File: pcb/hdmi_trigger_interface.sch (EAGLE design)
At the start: 60 parts, among them U1 TPD12S016PWR, U2 TPD12S016PWR, X1 87438-06, X2 87438-06, Y1 SI514

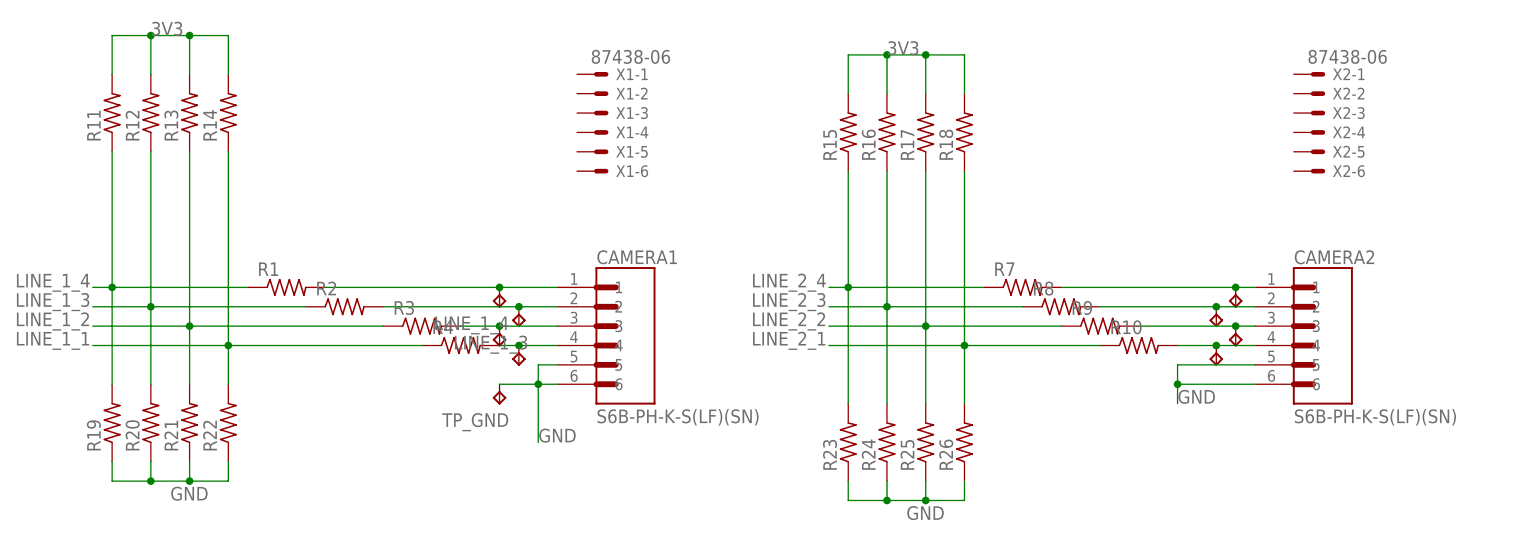
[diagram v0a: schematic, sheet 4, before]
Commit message: finished routing with new spacing and layout.
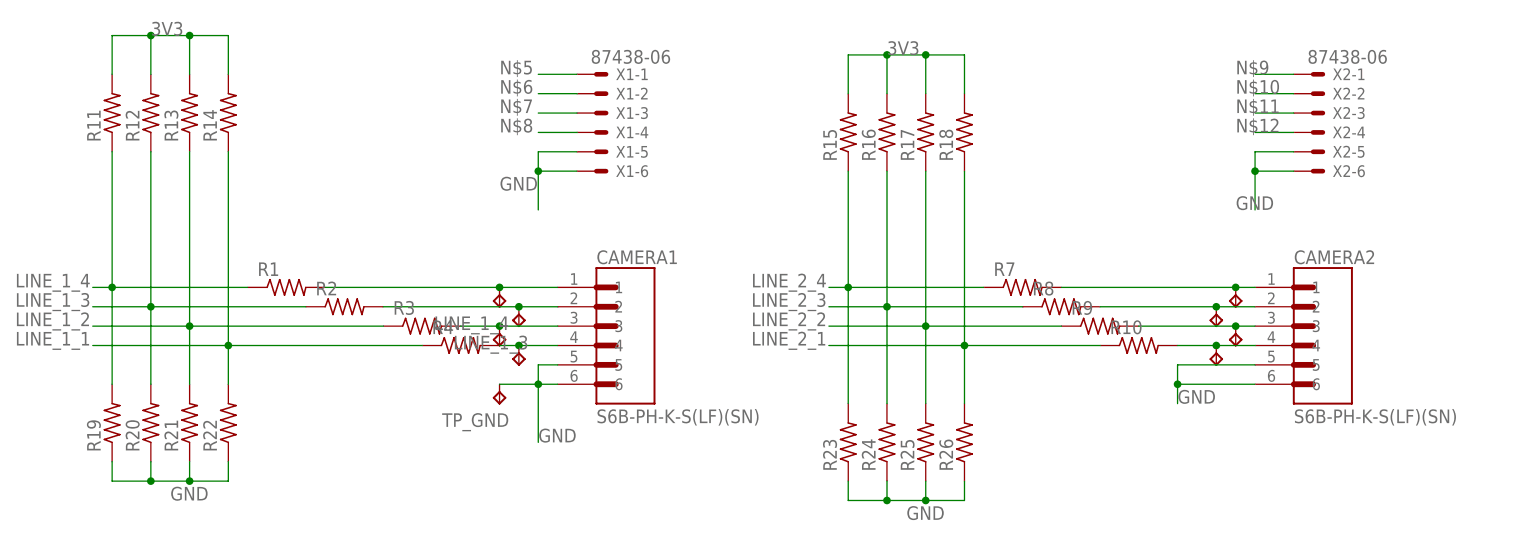
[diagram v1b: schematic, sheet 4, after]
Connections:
- net GND: now also X1-5.S, X1-6.S, X2-5.S, X2-6.S
- net N$10: now also X2-2.S
- net N$11: now also X2-3.S
- net N$12: now also X2-4.S
- net N$5: now also X1-1.S
- net N$6: now also X1-2.S
- net N$7: now also X1-3.S
- net N$8: now also X1-4.S
- net N$9: now also X2-1.S
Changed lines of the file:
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@@
 <label x="162.56" y="25.4" size="1.778" layer="95"/>
+</segment>
+<segment>
+<pinref part="X1" gate="-5" pin="S"/>
+<wire x1="83.82" y1="58.42" x2="78.74" y2="58.42" width="0.1524" layer="91"/>
+<wire x1="78.74" y1="58.42" x2="78.74" y2="55.88" width="0.1524" layer="91"/>
+<pinref part="X1" gate="-6" pin="S"/>
+<wire x1="78.74" y1="55.88" x2="83.82" y2="55.88" width="0.1524" layer="91"/>
+<wire x1="78.74" y1="55.88" x2="78.74" y2="50.8" width="0.1524" layer="91"/>
+<junction x="78.74" y="55.88"/>
+<label x="73.66" y="53.34" size="1.778" layer="95"/>
+</segment>
+<segment>
+<pinref part="X2" gate="-5" pin="S"/>
+<wire x1="177.8" y1="58.42" x2="172.72" y2="58.42" width="0.1524" layer="91"/>
+<wire x1="172.72" y1="58.42" x2="172.72" y2="55.88" width="0.1524" layer="91"/>
+<pinref part="X2" gate="-6" pin="S"/>
+<wire x1="172.72" y1="55.88" x2="177.8" y2="55.88" width="0.1524" layer="91"/>
+<wire x1="172.72" y1="55.88" x2="172.72" y2="50.8" width="0.1524" layer="91"/>
+<junction x="172.72" y="55.88"/>
+<label x="170.18" y="50.8" size="1.778" layer="95"/>
 </segment>
 </net>
@@
 <pinref part="CAMERA1" gate="G$1" pin="1"/>
 </segment>
+<segment>
+<pinref part="X1" gate="-1" pin="S"/>
+<wire x1="83.82" y1="68.58" x2="78.74" y2="68.58" width="0.1524" layer="91"/>
+<label x="73.66" y="68.58" size="1.778" layer="95"/>
+</segment>
 </net>
 <net name="N$6" class="0">
@@
 <pinref part="CAMERA1" gate="G$1" pin="2"/>
 </segment>
+<segment>
+<pinref part="X1" gate="-2" pin="S"/>
+<wire x1="83.82" y1="66.04" x2="78.74" y2="66.04" width="0.1524" layer="91"/>
+<label x="73.66" y="66.04" size="1.778" layer="95"/>
+</segment>
 </net>
 <net name="N$7" class="0">
@@
 <pinref part="CAMERA1" gate="G$1" pin="3"/>
 </segment>
+<segment>
+<pinref part="X1" gate="-3" pin="S"/>
+<wire x1="83.82" y1="63.5" x2="78.74" y2="63.5" width="0.1524" layer="91"/>
+<label x="73.66" y="63.5" size="1.778" layer="95"/>
+</segment>
 </net>
 <net name="N$8" class="0">
@@
 <pinref part="CAMERA1" gate="G$1" pin="4"/>
 </segment>
+<segment>
+<pinref part="X1" gate="-4" pin="S"/>
+<wire x1="83.82" y1="60.96" x2="78.74" y2="60.96" width="0.1524" layer="91"/>
+<label x="73.66" y="60.96" size="1.778" layer="95"/>
+</segment>
 </net>
 <net name="N$9" class="0">
@@
 <pinref part="CAMERA2" gate="G$1" pin="1"/>
 </segment>
+<segment>
+<pinref part="X2" gate="-1" pin="S"/>
+<wire x1="177.8" y1="68.58" x2="172.72" y2="68.58" width="0.1524" layer="91"/>
+<label x="170.18" y="68.58" size="1.778" layer="95"/>
+</segment>
 </net>
 <net name="N$10" class="0">
@@
 <pinref part="CAMERA2" gate="G$1" pin="2"/>
 </segment>
+<segment>
+<pinref part="X2" gate="-2" pin="S"/>
+<wire x1="177.8" y1="66.04" x2="172.72" y2="66.04" width="0.1524" layer="91"/>
+<label x="170.18" y="66.04" size="1.778" layer="95"/>
+</segment>
 </net>
 <net name="N$11" class="0">
@@
 <pinref part="CAMERA2" gate="G$1" pin="3"/>
 </segment>
+<segment>
+<pinref part="X2" gate="-3" pin="S"/>
+<wire x1="177.8" y1="63.5" x2="172.72" y2="63.5" width="0.1524" layer="91"/>
+<label x="170.18" y="63.5" size="1.778" layer="95"/>
+</segment>
 </net>
 <net name="N$12" class="0">
@@
 <pinref part="CAMERA2" gate="G$1" pin="4"/>
 </segment>
-</net>
+<segment>
+<pinref part="X2" gate="-4" pin="S"/>
+<wire x1="177.8" y1="60.96" x2="172.72" y2="60.96" width="0.1524" layer="91"/>
+<label x="170.18" y="60.96" size="1.778" layer="95"/>
+</segment>
+</net>
